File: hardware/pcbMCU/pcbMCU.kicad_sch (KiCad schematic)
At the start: 52 parts, among them J1 Conn_01x02, J2 Conn_01x04, J3 Conn_01x03, SW1 SW_SPDT, U1 AMS1117-3.3, Y1 32.768 KHz

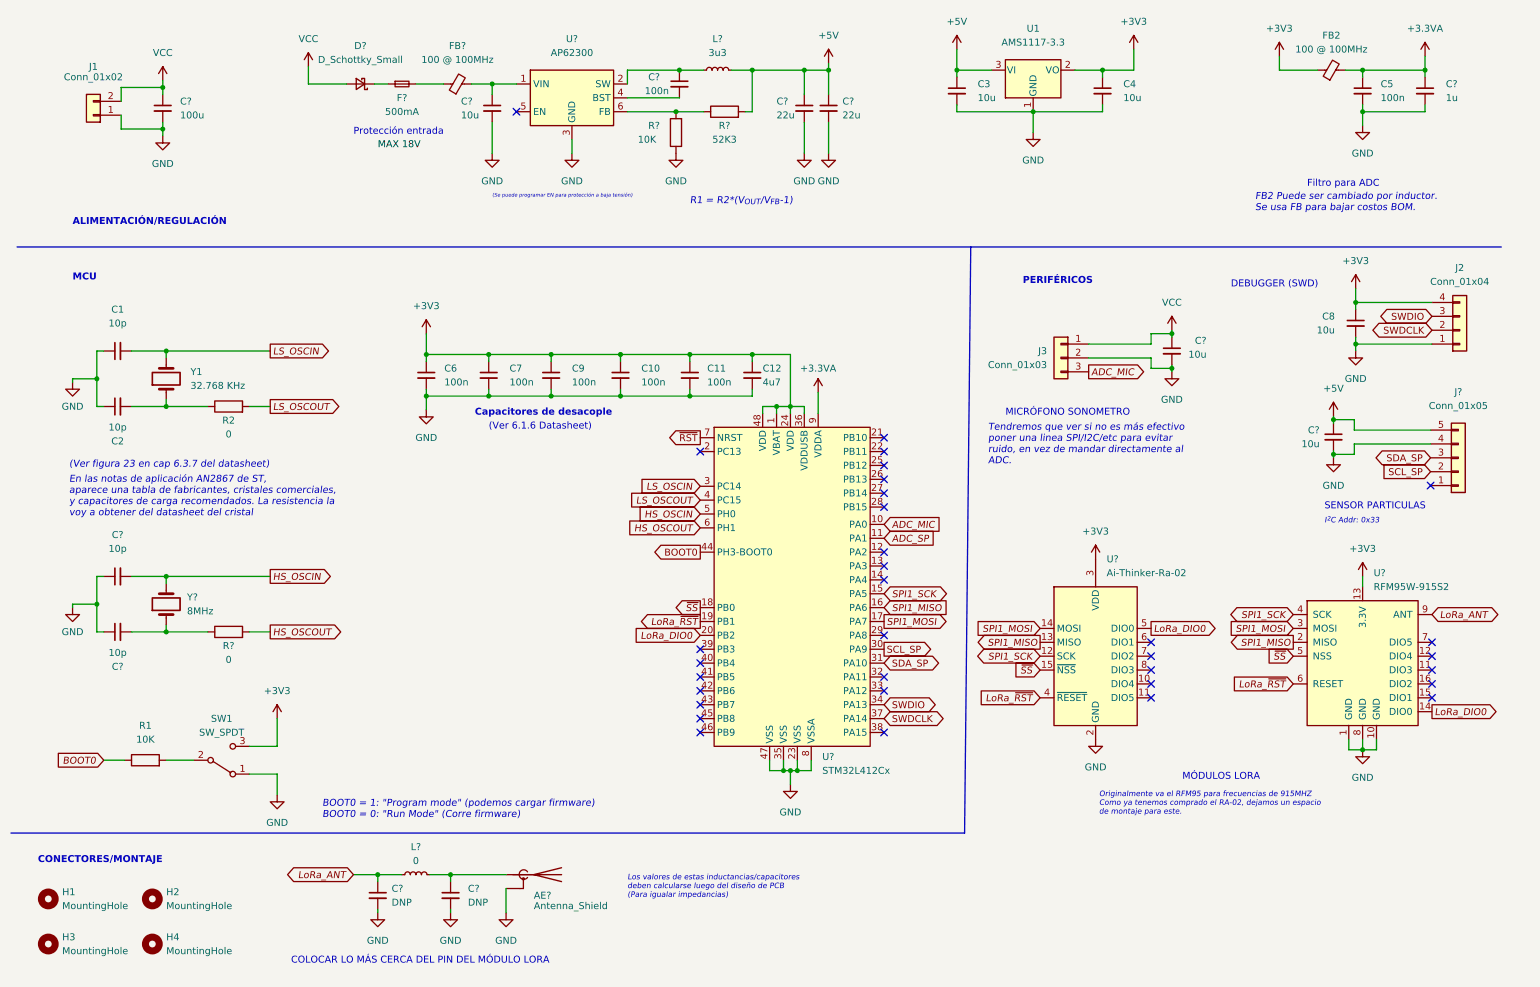
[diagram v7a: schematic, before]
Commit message: Footprint inicial de los componentes
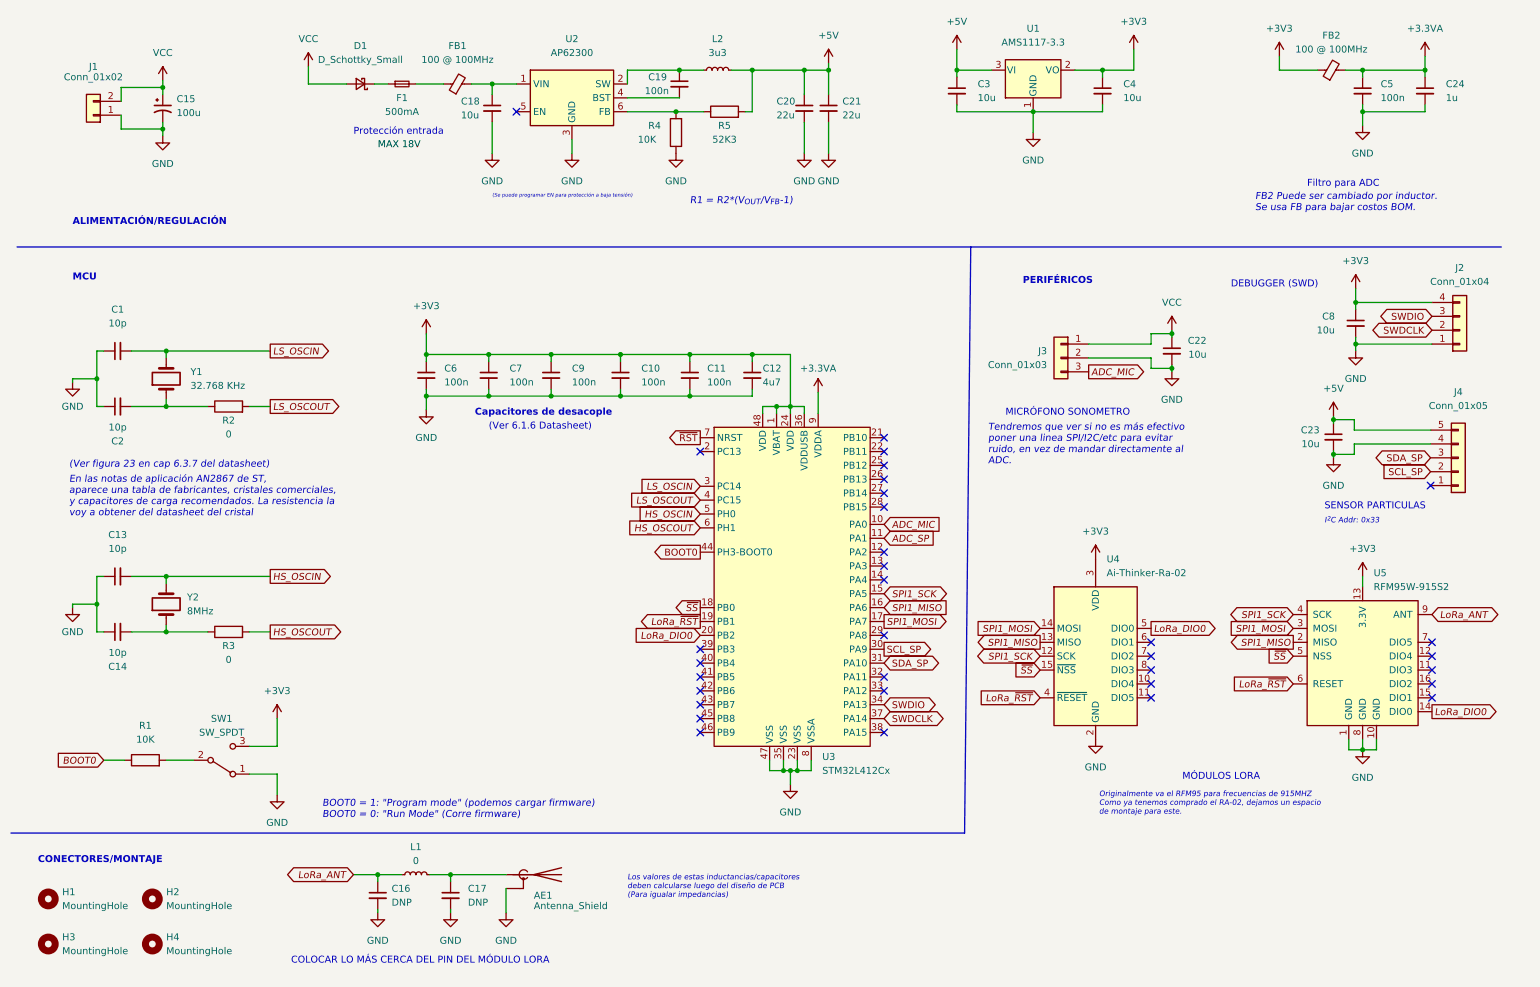
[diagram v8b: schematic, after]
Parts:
- removed C?: 100u, symbol Device:C_Small
- added C15: 100u, Capacitor_SMD:CP_Elec_6.3x5.7, symbol Device:C_Polarized_Small_US
- AE1: renamed from AE?; footprint (none) -> Connector_Coaxial:SMA_Amphenol_132203-12_Horizontal
- C1, C10, C11, C2, C5, C6, C7, C9: footprint (none) -> Capacitor_SMD:C_0603_1608Metric_Pad1.08x0.95mm_HandSolder
- C12, C3, C4, C8: footprint (none) -> Capacitor_SMD:C_0805_2012Metric_Pad1.18x1.45mm_HandSolder
- C13, C14, C16, C17, C19: renamed from C?; footprint (none) -> Capacitor_SMD:C_0603_1608Metric_Pad1.08x0.95mm_HandSolder
- C18, C20, C21, C22, C23, C24: renamed from C?; footprint (none) -> Capacitor_SMD:C_0805_2012Metric_Pad1.18x1.45mm_HandSolder
- D1: renamed from D?; footprint (none) -> Diode_SMD:D_0201_0603Metric_Pad0.64x0.40mm_HandSolder
- F1: renamed from F?; footprint (none) -> Fuse:Fuse_0603_1608Metric_Pad1.05x0.95mm_HandSolder
- FB1: renamed from FB?; footprint (none) -> Inductor_SMD:L_0603_1608Metric_Pad1.05x0.95mm_HandSolder
- FB2: footprint (none) -> Inductor_SMD:L_0603_1608Metric_Pad1.05x0.95mm_HandSolder
- H1, H2, H3, H4: footprint (none) -> MountingHole:MountingHole_5mm_Pad_Via
- J1: footprint (none) -> Connector_PinSocket_2.54mm:PinSocket_1x02_P2.54mm_Vertical
- J2: footprint (none) -> Connector_PinHeader_1.27mm:PinHeader_1x04_P1.27mm_Vertical
- J3: footprint (none) -> Connector_JST:JST_GH_SM03B-GHS-TB_1x03-1MP_P1.25mm_Horizontal
- L1, L2: renamed from L?; footprint (none) -> Inductor_SMD:L_0603_1608Metric_Pad1.05x0.95mm_HandSolder
- R1, R2: footprint (none) -> Resistor_SMD:R_0603_1608Metric_Pad0.98x0.95mm_HandSolder
- R3, R4, R5: renamed from R?; footprint (none) -> Resistor_SMD:R_0603_1608Metric_Pad0.98x0.95mm_HandSolder
- SW1: footprint (none) -> Connector_PinHeader_1.27mm:PinHeader_1x03_P1.27mm_Vertical
- U3: renamed from U?; footprint (none) -> Package_QFP:LQFP-48-1EP_7x7mm_P0.5mm_EP3.6x3.6mm_ThermalVias
- U5: renamed from U?; footprint (none) -> pcbMCU:XCVR_RFM95W-915S2
- Y1: footprint (none) -> Crystal:Crystal_SMD_0603-2Pin_6.0x3.5mm_HandSoldering
- Y2: renamed from Y?; footprint (none) -> Crystal:Crystal_SMD_0603-2Pin_6.0x3.5mm_HandSoldering
- gave numbers to parts that had none: 3
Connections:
- net GND: now also C15.2
- net VCC: now also C15.1
